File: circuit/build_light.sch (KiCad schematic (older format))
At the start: 10 parts, among them Q1 2N3904, Q2 2N3904, Q3 2N3904, U1 TOWER

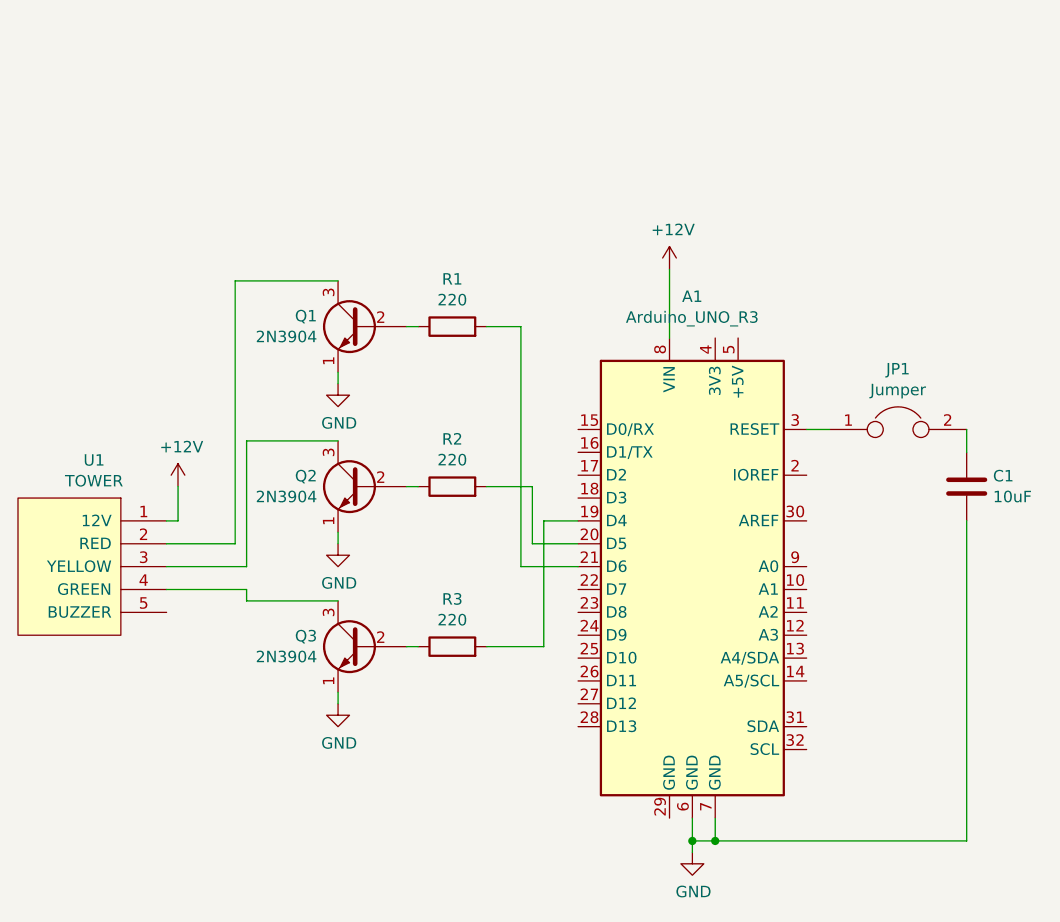
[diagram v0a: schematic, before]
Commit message: added boost converter to replace the external 12V power supply
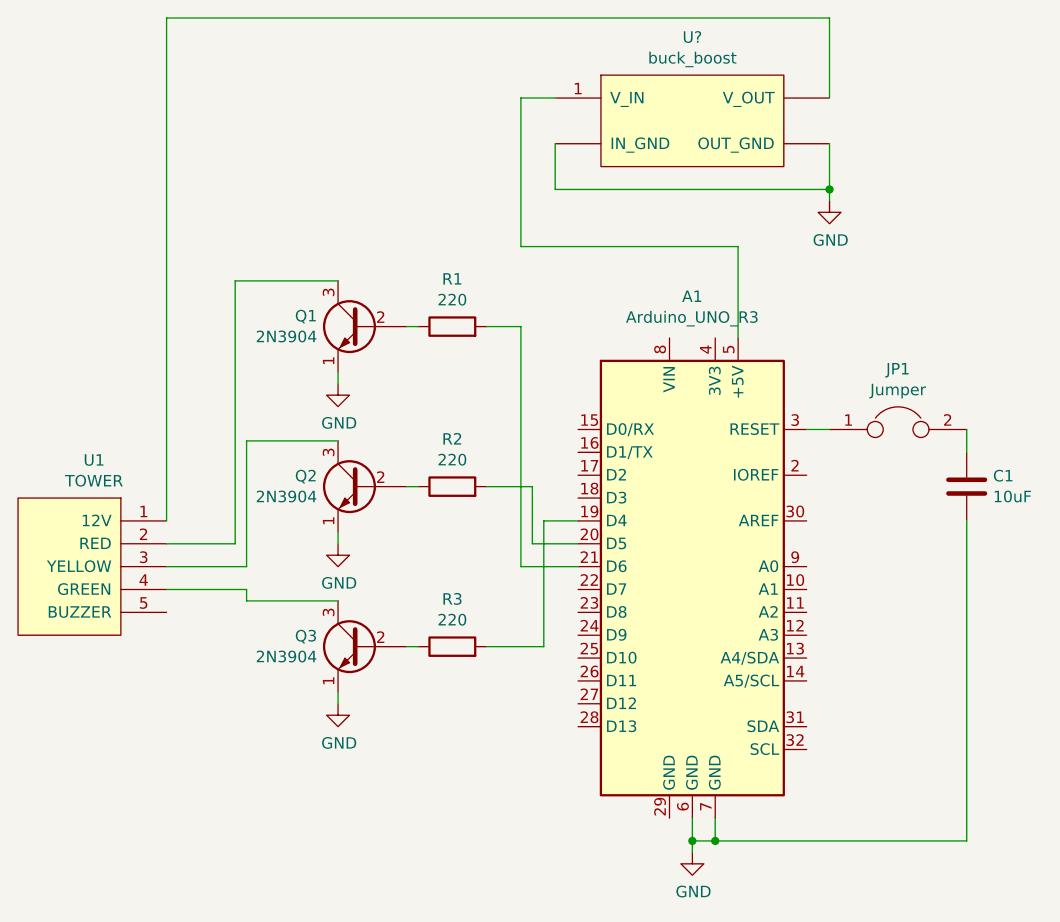
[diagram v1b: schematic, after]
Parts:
- added U?: buck_boost, symbol light_tower:buck_boost
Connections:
- net GND: now also U?.~ (V_OUT)
- net at A1.5 (+5V): now also U?.1 (V_IN)
- net +12V: no longer names the net of A1.8 (VIN)
- net +12V: no longer U1.1 (12V)
- new net: U1.1 (12V), U?.~ (V_OUT)
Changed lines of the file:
@@
-$EndComp
-$Comp
-L power:+12V #PWR06
-U 1 1 5D7CF0A5
-P 6400 2850
-F 0 "#PWR06" H 6400 2700 50  0001 C CNN
-F 1 "+12V" H 6415 3023 50  0000 C CNN
-F 2 "" H 6400 2850 50  0001 C CNN
-F 3 "" H 6400 2850 50  0001 C CNN
-	1    6400 2850
-	1    0    0    -1
 $EndComp
 $Comp
@@
 	0    -1   -1   0
 $EndComp
-$Comp
-L power:+12V #PWR01
-U 1 1 5D7D7F5C
-P 4250 3800
-F 0 "#PWR01" H 4250 3650 50  0001 C CNN
-F 1 "+12V" H 4265 3973 50  0000 C CNN
-F 2 "" H 4250 3800 50  0001 C CNN
-F 3 "" H 4250 3800 50  0001 C CNN
-	1    4250 3800
-	1    0    0    -1
-$EndComp
 Wire Wire Line
 	4950 3300 4950 3350
@@
 Wire Wire Line
 	4500 4050 4200 4050
-Wire Wire Line
-	6400 2850 6400 3150
 Wire Wire Line
 	6500 5350 6500 5400
@@
 	7700 5350 6600 5350
 Connection ~ 6600 5350
-Wire Wire Line
-	4200 3950 4250 3950
-Wire Wire Line
-	4250 3950 4250 3800
+$Comp
+L light_tower:buck_boost U?
+U 1 1 5D92E78D
+P 6300 1900
+F 0 "U?" H 6500 1965 50  0000 C CNN
+F 1 "buck_boost" H 6500 1874 50  0000 C CNN
+F 2 "" H 6300 1900 50  0001 C CNN
+F 3 "" H 6300 1900 50  0001 C CNN
+	1    6300 1900
+	1    0    0    -1
+$EndComp
+$Comp
+L power:GND #PWR?
+U 1 1 5D92F05E
+P 7100 2550
+F 0 "#PWR?" H 7100 2300 50  0001 C CNN
+F 1 "GND" H 7105 2377 50  0000 C CNN
+F 2 "" H 7100 2550 50  0001 C CNN
+F 3 "" H 7100 2550 50  0001 C CNN
+	1    7100 2550
+	1    0    0    -1
+$EndComp
+Wire Wire Line
+	5900 2300 5900 2500
+Wire Wire Line
+	5900 2500 7100 2500
+Wire Wire Line
+	7100 2500 7100 2300
+Wire Wire Line
+	7100 2500 7100 2550
+Connection ~ 7100 2500
+Wire Wire Line
+	6700 3150 6700 2750
+Wire Wire Line
+	6700 2750 5750 2750
+Wire Wire Line
+	5750 2750 5750 2100
+Wire Wire Line
+	5750 2100 5900 2100
+Wire Wire Line
+	7100 2100 7100 1750
+Wire Wire Line
+	7100 1750 4200 1750
+Wire Wire Line
+	4200 1750 4200 3950
 $EndSCHEMATC
